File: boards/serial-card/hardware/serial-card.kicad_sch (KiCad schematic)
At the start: 62 parts, among them J10 STACK BUS, J11 RACK 12V, J20 RS-232 1, J21 RS-232 2, J30 RS-485 3, J31 RS-485 4, U1 ST3232B, U10 ISOW1432, U11 ISOW1432

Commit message: Rev A order files; serial-card box headers checked against the vendor model
docs/orders: DigiKey upload CSV for one set of the six boards to order
(core, can-card, io-card, serial-card, can-ssr, probe-helper: 121 lines,
450 parts) and a README listing the items not in the board BOMs
(mating plugs, shunts, cables, standoffs) plus the assembly note below.

serial-card J20/J21/J30/J31 use Thl_Connector:Amphenol_T821110A1R100CEU_
2x05_P2.54mm_Horizontal (stock IDC pads, which match Amphenol's land
pattern, plus the SamacSys STEP from transfer/, kept local per its
licence). The body is 8.86 mm (the stock model showed 11.1 mm), leaving
2.3 mm under the next board (ESQ-120-14, 11.18 mm); THT tails of the board
above land over the headers in every stack order, so tails under the
stack boards are trimmed to about 1.5 mm.

io-card README: AQW212 is the AC/DC type, so off outputs block a reversed
coil supply.

Co-Authored-By: Claude Opus 5.5 <noreply@anthropic.com>
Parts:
- J20, J21, J30, J31: footprint Connector_IDC:IDC-Header_2x05_P2.54mm_Horizontal -> Thl_Connector:Amphenol_T821110A1R100CEU_2x05_P2.54mm_Horizontal
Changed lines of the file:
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@@
 			)
 		)
-		(property "Footprint" "Connector_IDC:IDC-Header_2x05_P2.54mm_Horizontal"
+		(property "Footprint" "Thl_Connector:Amphenol_T821110A1R100CEU_2x05_P2.54mm_Horizontal"
 			(at 165.1 63.5 0)
 			(hide yes)
@@
 			)
 		)
-		(property "Footprint" "Connector_IDC:IDC-Header_2x05_P2.54mm_Horizontal"
+		(property "Footprint" "Thl_Connector:Amphenol_T821110A1R100CEU_2x05_P2.54mm_Horizontal"
 			(at 165.1 99.06 0)
 			(hide yes)
@@
 			)
 		)
-		(property "Footprint" "Connector_IDC:IDC-Header_2x05_P2.54mm_Horizontal"
+		(property "Footprint" "Thl_Connector:Amphenol_T821110A1R100CEU_2x05_P2.54mm_Horizontal"
 			(at 297.18 160.02 0)
 			(hide yes)
@@
 			)
 		)
-		(property "Footprint" "Connector_IDC:IDC-Header_2x05_P2.54mm_Horizontal"
+		(property "Footprint" "Thl_Connector:Amphenol_T821110A1R100CEU_2x05_P2.54mm_Horizontal"
 			(at 297.18 236.22 0)
 			(hide yes)

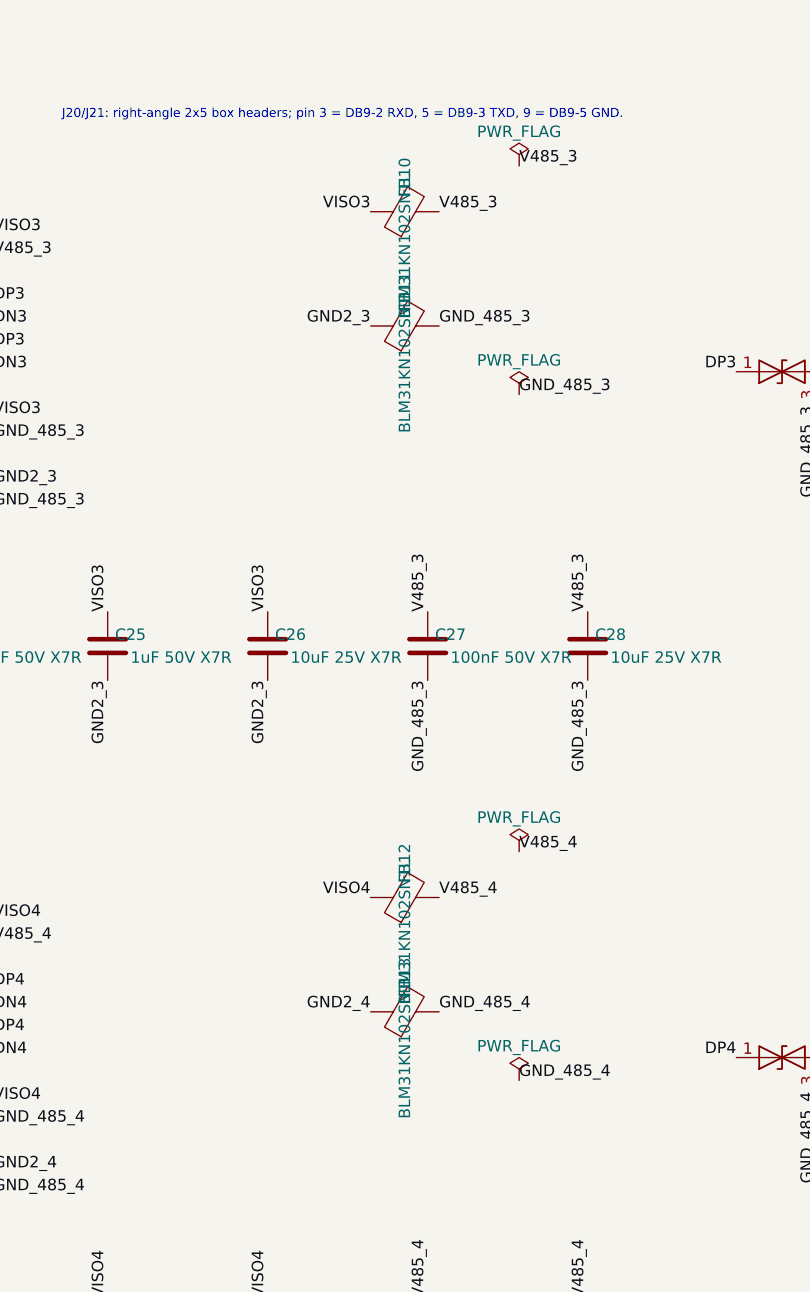
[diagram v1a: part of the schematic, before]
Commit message: Move core, can-card, io-card, serial-card, can-ssr, probe-helper to rev B
Rev A went to PCBWay and is tagged revA. Rev B replaces parts the Mouser
BOM check flagged (obsolete, end of life, not recommended for new designs,
or not orderable) and swaps out-of-stock passives and diodes for in-stock
equivalents. Field-only changes, same footprints, no layout change; the
reference boards (can-controller, pic-module) get the same part numbers.
The rev A order lists (DigiKey, Mouser) carry the same substitutions; the
Mouser list leaves out the T821 box headers (bought from DigiKey).

docs/rev-b-changes.md lists every change and the rev B to-dos (MAX7219 is
obsolete and must be replaced). transfer/mouser-revA.xlsx (Mouser BOM
check) consumed.

Co-Authored-By: Claude Opus 5.5 <noreply@anthropic.com>
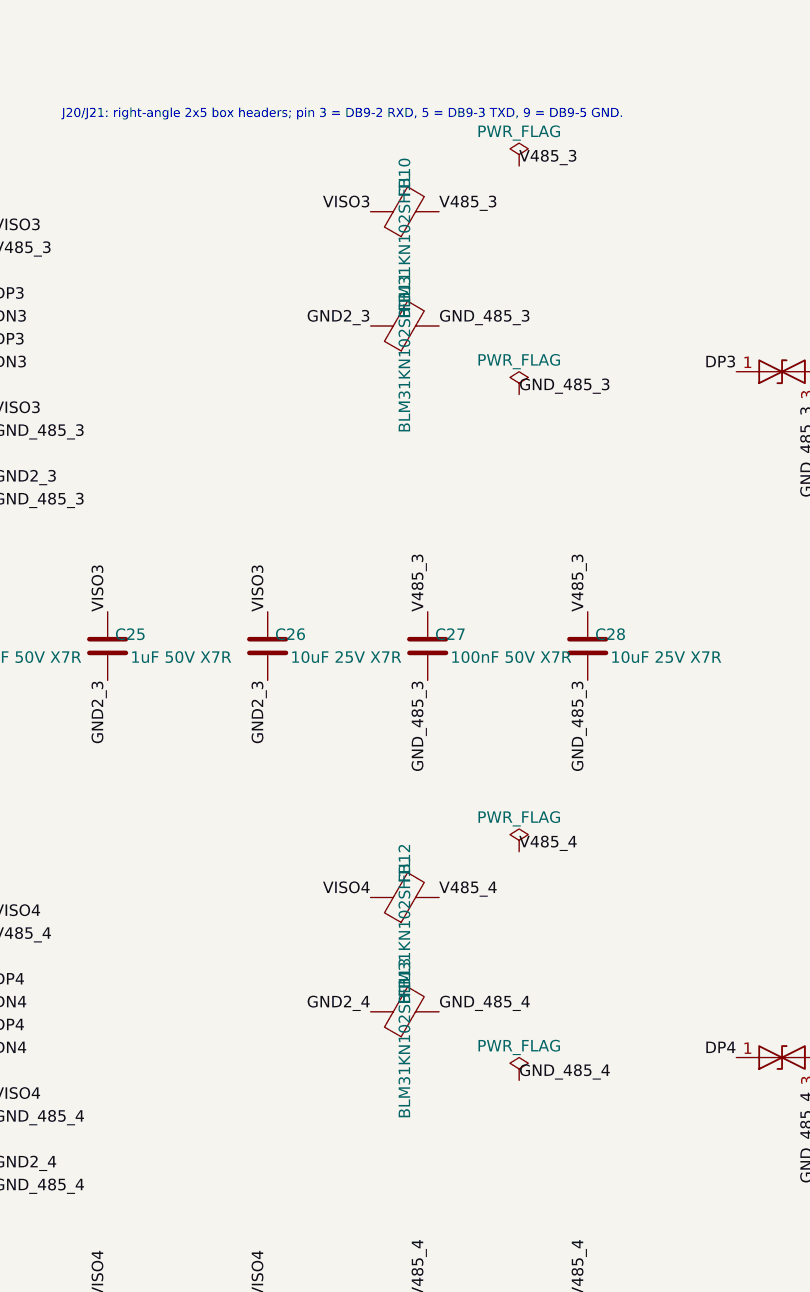
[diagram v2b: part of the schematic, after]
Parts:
- C1, C2, C3, C4: MPN GRM319R71H104KA01D -> C1206C104K5RACTU; Manufacturer Murata -> KEMET
- C20, C27, C30, C37, C5: MPN GRM21BR71H104KA01L -> C0805C104K5RACTU; Manufacturer Murata -> KEMET
- C21, C24, C31, C34: MPN GRM21BR71H103KA01L -> C0805C103K5RACTU; Manufacturer Murata -> KEMET
- C22, C25, C32, C35: MPN GRM31MR71H105KA88L -> C1206C105K5RACTU; Manufacturer Murata -> KEMET
- C23, C26, C28, C33, C36, C38, C6, C7: MPN GRM31CR71E106KA12L -> CL31B106KAHNNNE; Manufacturer Murata -> Samsung Electro-Mechanics
- D1, D3, D5, D7: MPN LTST-C150GKT -> LTST-C150KGKT
- FB10, FB11, FB12, FB13: value BLM31KN102SN1L -> BLM31KN102SH1L; MPN BLM31KN102SN1L -> BLM31KN102SH1L
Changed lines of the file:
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@@
 		(title "Serial card: 2 x RS-232, 2 x isolated RS-485")
 		(date "2026-10-09")
-		(rev "A")
+		(rev "B")
 	)
 	(text "RS-232 ports 1 and 2 (UART2, UART3): ST3232B, 3.3 V, +-15 kV ESD on the bus pins, not isolated\n(decided 2026-10-09). 3-wire: DB9 2 RXD (in), 3 TXD (out), 5 GND (DTE, male DB9 on the adapter).\nNo handshake lines: a device that needs them gets them looped in its cable."
@@
 			)
 		)
-		(property "Manufacturer" "Murata"
+		(property "Manufacturer" "KEMET"
 			(at 45.72 60.96 0)
 			(hide yes)
@@
 			)
 		)
-		(property "MPN" "GRM319R71H104KA01D"
+		(property "MPN" "C1206C104K5RACTU"
 			(at 45.72 60.96 0)
 			(hide yes)
@@
 			)
 		)
-		(property "Manufacturer" "Murata"
+		(property "Manufacturer" "KEMET"
 			(at 66.04 60.96 0)
 			(hide yes)
@@
 			)
 		)
-		(property "MPN" "GRM319R71H104KA01D"
+		(property "MPN" "C1206C104K5RACTU"
 			(at 66.04 60.96 0)
 			(hide yes)
@@
 			)
 		)
-		(property "Manufacturer" "Murata"
+		(property "Manufacturer" "KEMET"
 			(at 45.72 83.82 0)
 			(hide yes)
@@
 			)
 		)
-		(property "MPN" "GRM319R71H104KA01D"
+		(property "MPN" "C1206C104K5RACTU"
 			(at 45.72 83.82 0)
 			(hide yes)
@@
 			)
 		)
-		(property "Manufacturer" "Murata"
+		(property "Manufacturer" "KEMET"
 			(at 66.04 83.82 0)
 			(hide yes)
@@
 			)
 		)
-		(property "MPN" "GRM319R71H104KA01D"
+		(property "MPN" "C1206C104K5RACTU"
 			(at 66.04 83.82 0)
 			(hide yes)
@@
 			)
 		)
-		(property "Manufacturer" "Murata"
+		(property "Manufacturer" "KEMET"
 			(at 124.46 35.56 0)
 			(hide yes)
@@
 			)
 		)
-		(property "MPN" "GRM21BR71H104KA01L"
+		(property "MPN" "C0805C104K5RACTU"
 			(at 124.46 35.56 0)
 			(hide yes)
@@
 			)
 		)
-		(property "Manufacturer" "Murata"
+		(property "Manufacturer" "KEMET"
 			(at 50.8 190.5 0)
 			(hide yes)
@@
 			)
 		)
-		(property "MPN" "GRM21BR71H104KA01L"
+		(property "MPN" "C0805C104K5RACTU"
 			(at 50.8 190.5 0)
 			(hide yes)
@@
 			)
 		)
-		(property "Manufacturer" "Murata"
+		(property "Manufacturer" "KEMET"
 			(at 68.58 190.5 0)
 			(hide yes)
@@
 			)
 		)
-		(property "MPN" "GRM21BR71H103KA01L"
+		(property "MPN" "C0805C103K5RACTU"
 			(at 68.58 190.5 0)
 			(hide yes)
@@
 			)
 		)
-		(property "Manufacturer" "Murata"
+		(property "Manufacturer" "KEMET"
 			(at 86.36 190.5 0)
 			(hide yes)
@@
 			)
 		)
-		(property "MPN" "GRM31MR71H105KA88L"
+		(property "MPN" "C1206C105K5RACTU"
 			(at 86.36 190.5 0)
 			(hide yes)
@@
 			)
 		)
-		(property "Manufacturer" "Murata"
+		(property "Manufacturer" "Samsung Electro-Mechanics"
 			(at 104.14 190.5 0)
 			(hide yes)
@@
 			)
 		)
-		(property "MPN" "GRM31CR71E106KA12L"
+		(property "MPN" "CL31B106KAHNNNE"
 			(at 104.14 190.5 0)
 			(hide yes)
@@
 			)
 		)
-		(property "Manufacturer" "Murata"
+		(property "Manufacturer" "KEMET"
 			(at 127 190.5 0)
 			(hide yes)
@@
 			)
 		)
-		(property "MPN" "GRM21BR71H103KA01L"
+		(property "MPN" "C0805C103K5RACTU"
 			(at 127 190.5 0)
 			(hide yes)
@@
 			)
 		)
-		(property "Manufacturer" "Murata"
+		(property "Manufacturer" "KEMET"
 			(at 144.78 190.5 0)
 			(hide yes)
@@
 			)
 		)
-		(property "MPN" "GRM31MR71H105KA88L"
+		(property "MPN" "C1206C105K5RACTU"
 			(at 144.78 190.5 0)
 			(hide yes)
@@
 			)
 		)
-		(property "Manufacturer" "Murata"
+		(property "Manufacturer" "Samsung Electro-Mechanics"
 			(at 162.56 190.5 0)
 			(hide yes)
@@
 			)
 		)
-		(property "MPN" "GRM31CR71E106KA12L"
+		(property "MPN" "CL31B106KAHNNNE"
 			(at 162.56 190.5 0)
 			(hide yes)
@@
 			)
 		)
-		(property "Value" "BLM31KN102SN1L"
+		(property "Value" "BLM31KN102SH1L"
 			(at 177.8 146.05 0)
 			(effects
@@
 			)
 		)
-		(property "MPN" "BLM31KN102SN1L"
+		(property "MPN" "BLM31KN102SH1L"
 			(at 177.8 142.24 0)
 			(hide yes)
@@
 			)
 		)
-		(property "Value" "BLM31KN102SN1L"
+		(property "Value" "BLM31KN102SH1L"
 			(at 177.8 158.75 0)
 			(effects
@@
 			)
 		)
-		(property "MPN" "BLM31KN102SN1L"
+		(property "MPN" "BLM31KN102SH1L"
 			(at 177.8 154.94 0)
 			(hide yes)
@@
 			)
 		)
-		(property "Manufacturer" "Murata"
+		(property "Manufacturer" "KEMET"
 			(at 180.34 190.5 0)
 			(hide yes)
@@
 			)
 		)
-		(property "MPN" "GRM21BR71H104KA01L"
+		(property "MPN" "C0805C104K5RACTU"
 			(at 180.34 190.5 0)
 			(hide yes)
@@
 			)
 		)
-		(property "Manufacturer" "Murata"
+		(property "Manufacturer" "Samsung Electro-Mechanics"
 			(at 198.12 190.5 0)
 			(hide yes)
@@
 			)
 		)
-		(property "MPN" "GRM31CR71E106KA12L"
+		(property "MPN" "CL31B106KAHNNNE"
 			(at 198.12 190.5 0)
 			(hide yes)
@@
 			)
 		)
-		(property "Manufacturer" "Murata"
+		(property "Manufacturer" "KEMET"
 			(at 50.8 266.7 0)
 			(hide yes)
@@
 			)
 		)
-		(property "MPN" "GRM21BR71H104KA01L"
+		(property "MPN" "C0805C104K5RACTU"
 			(at 50.8 266.7 0)
 			(hide yes)
@@
 			)
 		)
-		(property "Manufacturer" "Murata"
+		(property "Manufacturer" "KEMET"
 			(at 68.58 266.7 0)
 			(hide yes)
@@
 			)
 		)
-		(property "MPN" "GRM21BR71H103KA01L"
+		(property "MPN" "C0805C103K5RACTU"
 			(at 68.58 266.7 0)
 			(hide yes)
@@
 			)
 		)
-		(property "Manufacturer" "Murata"
+		(property "Manufacturer" "KEMET"
 			(at 86.36 266.7 0)
 			(hide yes)
@@
 			)
 		)
-		(property "MPN" "GRM31MR71H105KA88L"
+		(property "MPN" "C1206C105K5RACTU"
 			(at 86.36 266.7 0)
 			(hide yes)
@@
 			)
 		)
-		(property "Manufacturer" "Murata"
+		(property "Manufacturer" "Samsung Electro-Mechanics"
 			(at 104.14 266.7 0)
 			(hide yes)
@@
 			)
 		)
-		(property "MPN" "GRM31CR71E106KA12L"
+		(property "MPN" "CL31B106KAHNNNE"
 			(at 104.14 266.7 0)
 			(hide yes)
@@
 			)
 		)
-		(property "Manufacturer" "Murata"
+		(property "Manufacturer" "KEMET"
 			(at 127 266.7 0)
 			(hide yes)
@@
 			)
 		)
-		(property "MPN" "GRM21BR71H103KA01L"
+		(property "MPN" "C0805C103K5RACTU"
 			(at 127 266.7 0)
 			(hide yes)
@@
 			)
 		)
-		(property "Manufacturer" "Murata"
+		(property "Manufacturer" "KEMET"
 			(at 144.78 266.7 0)
 			(hide yes)
@@
 			)
 		)
-		(property "MPN" "GRM31MR71H105KA88L"
+		(property "MPN" "C1206C105K5RACTU"
 			(at 144.78 266.7 0)
 			(hide yes)
@@
 			)
 		)
-		(property "Manufacturer" "Murata"
+		(property "Manufacturer" "Samsung Electro-Mechanics"
 			(at 162.56 266.7 0)
 			(hide yes)
@@
 			)
 		)
-		(property "MPN" "GRM31CR71E106KA12L"
+		(property "MPN" "CL31B106KAHNNNE"
 			(at 162.56 266.7 0)
 			(hide yes)
@@
 			)
 		)
-		(property "Value" "BLM31KN102SN1L"
+		(property "Value" "BLM31KN102SH1L"
 			(at 177.8 222.25 0)
 			(effects
@@
 			)
 		)
-		(property "MPN" "BLM31KN102SN1L"
+		(property "MPN" "BLM31KN102SH1L"
 			(at 177.8 218.44 0)
 			(hide yes)
@@
 			)
 		)
-		(property "Value" "BLM31KN102SN1L"
+		(property "Value" "BLM31KN102SH1L"
 			(at 177.8 234.95 0)
 			(effects
@@
 			)
 		)
-		(property "MPN" "BLM31KN102SN1L"
+		(property "MPN" "BLM31KN102SH1L"
 			(at 177.8 231.14 0)
 			(hide yes)
@@
 			)
 		)
-		(property "Manufacturer" "Murata"
+		(property "Manufacturer" "KEMET"
 			(at 180.34 266.7 0)
 			(hide yes)
@@
 			)
 		)
-		(property "MPN" "GRM21BR71H104KA01L"
+		(property "MPN" "C0805C104K5RACTU"
 			(at 180.34 266.7 0)
 			(hide yes)
@@
 			)
 		)
-		(property "Manufacturer" "Murata"
+		(property "Manufacturer" "Samsung Electro-Mechanics"
 			(at 198.12 266.7 0)
 			(hide yes)
@@
 			)
 		)
-		(property "MPN" "GRM31CR71E106KA12L"
+		(property "MPN" "CL31B106KAHNNNE"
 			(at 198.12 266.7 0)
 			(hide yes)
@@
 			)
 		)
-		(property "MPN" "LTST-C150GKT"
+		(property "MPN" "LTST-C150KGKT"
 			(at 233.68 43.18 0)
 			(hide yes)
@@
 			)
 		)
-		(property "MPN" "LTST-C150GKT"
+		(property "MPN" "LTST-C150KGKT"
 			(at 264.16 43.18 0)
 			(hide yes)
@@
 			)
 		)
-		(property "MPN" "LTST-C150GKT"
+		(property "MPN" "LTST-C150KGKT"
 			(at 233.68 71.12 0)
 			(hide yes)
@@
 			)
 		)
-		(property "MPN" "LTST-C150GKT"
+		(property "MPN" "LTST-C150KGKT"
 			(at 264.16 71.12 0)
 			(hide yes)
@@
 			)
 		)
-		(property "Manufacturer" "Murata"
+		(property "Manufacturer" "Samsung Electro-Mechanics"
 			(at 342.9 190.5 0)
 			(hide yes)
@@
 			)
 		)
-		(property "MPN" "GRM31CR71E106KA12L"
+		(property "MPN" "CL31B106KAHNNNE"
 			(at 342.9 190.5 0)
 			(hide yes)
@@
 			)
 		)
-		(property "Manufacturer" "Murata"
+		(property "Manufacturer" "Samsung Electro-Mechanics"
 			(at 363.22 190.5 0)
 			(hide yes)
@@
 			)
 		)
-		(property "MPN" "GRM31CR71E106KA12L"
+		(property "MPN" "CL31B106KAHNNNE"
 			(at 363.22 190.5 0)
 			(hide yes)
